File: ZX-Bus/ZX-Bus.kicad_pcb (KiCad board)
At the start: 2 copper layers, 177 x 146 mm, 56 parts, among them J1 DIP-40 Pins, J10 DIP14, J11 PBS-4, J12 PBS-5, J2 PLS-3, J3 PLS-6, J4 Power, J5 Main board power, J6 12V, J7 5V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

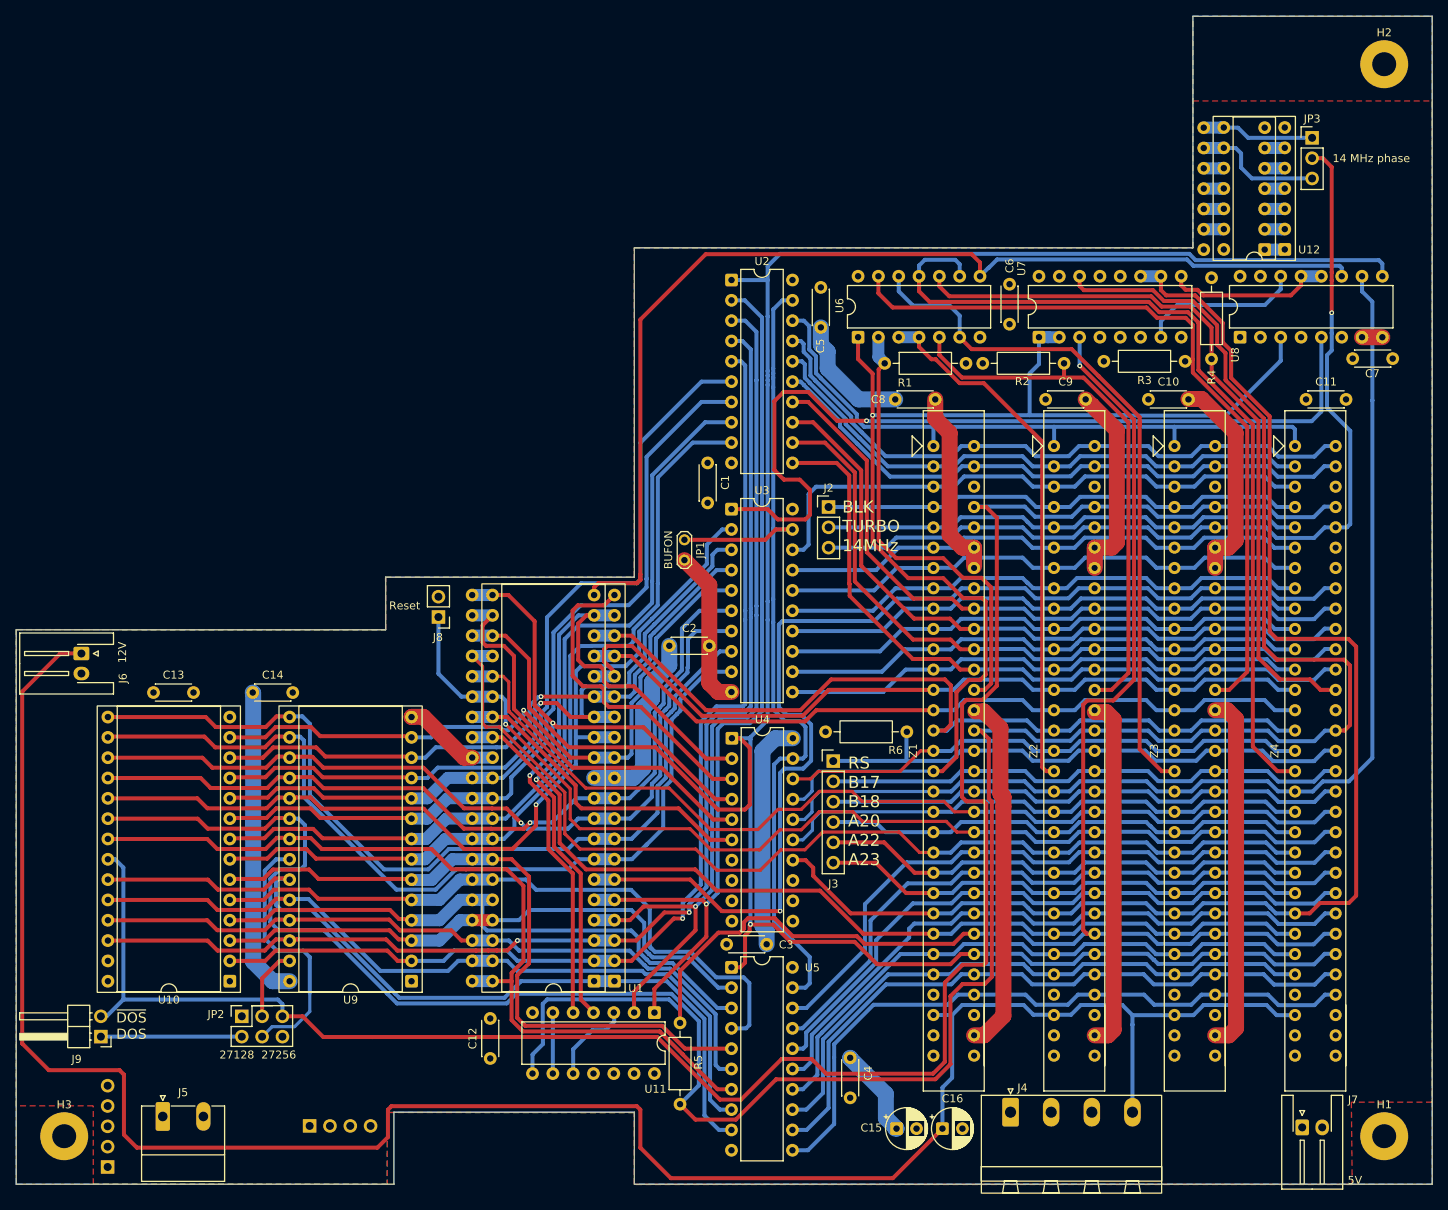
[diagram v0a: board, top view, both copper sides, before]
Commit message: ZX-Bus: Correct mounting hole placement
Based on mockup testing and re-measurement
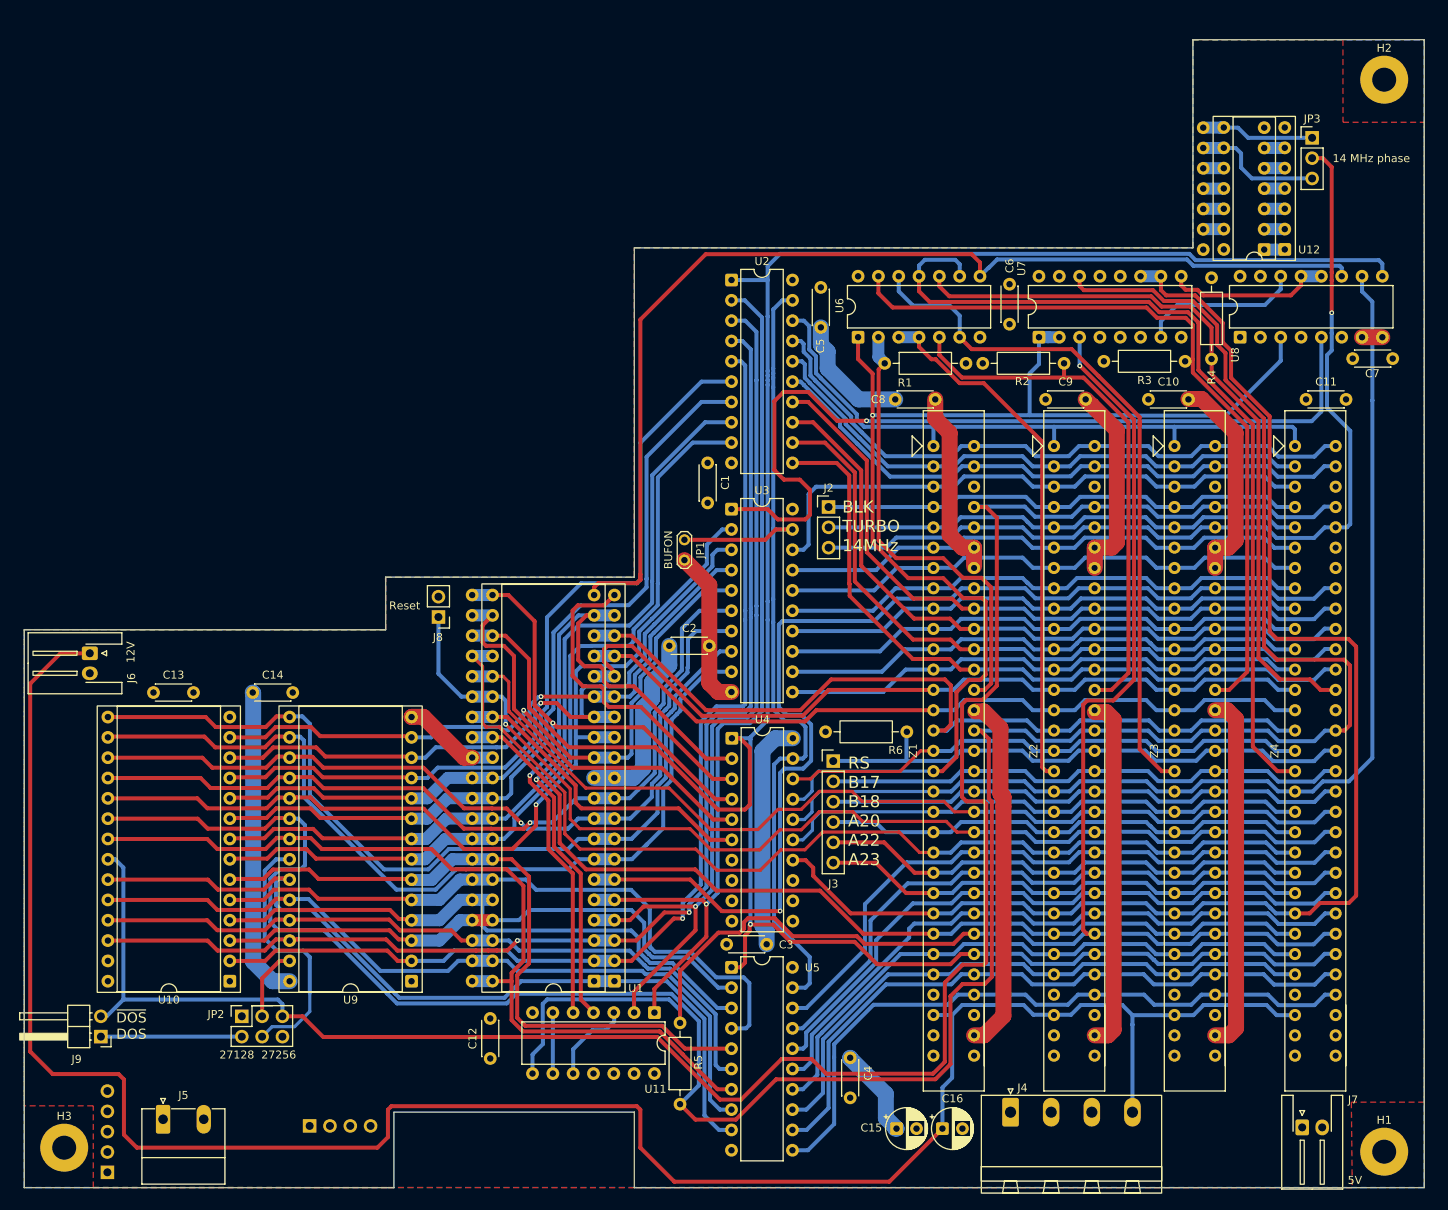
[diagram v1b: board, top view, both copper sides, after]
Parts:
- moved H1 1.94 mm to (186.8, 196.7)
- moved H2 1.94 mm to (186.8, 62.7)
- moved H3 1.44 mm to (21.8, 196.2)
- moved J6 1.05 mm to (25.0, 134.4)
- moved J12 0.67 mm to (27.2, 199.3)
- moved J5 0.35 mm to (34.1, 192.7)
- moved J10 0.06 mm to (171.8, 84.0)
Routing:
- net +12V: track 266.5 -> 265.7 mm
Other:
- board size 177 x 146 mm -> 175 x 143.5 mm

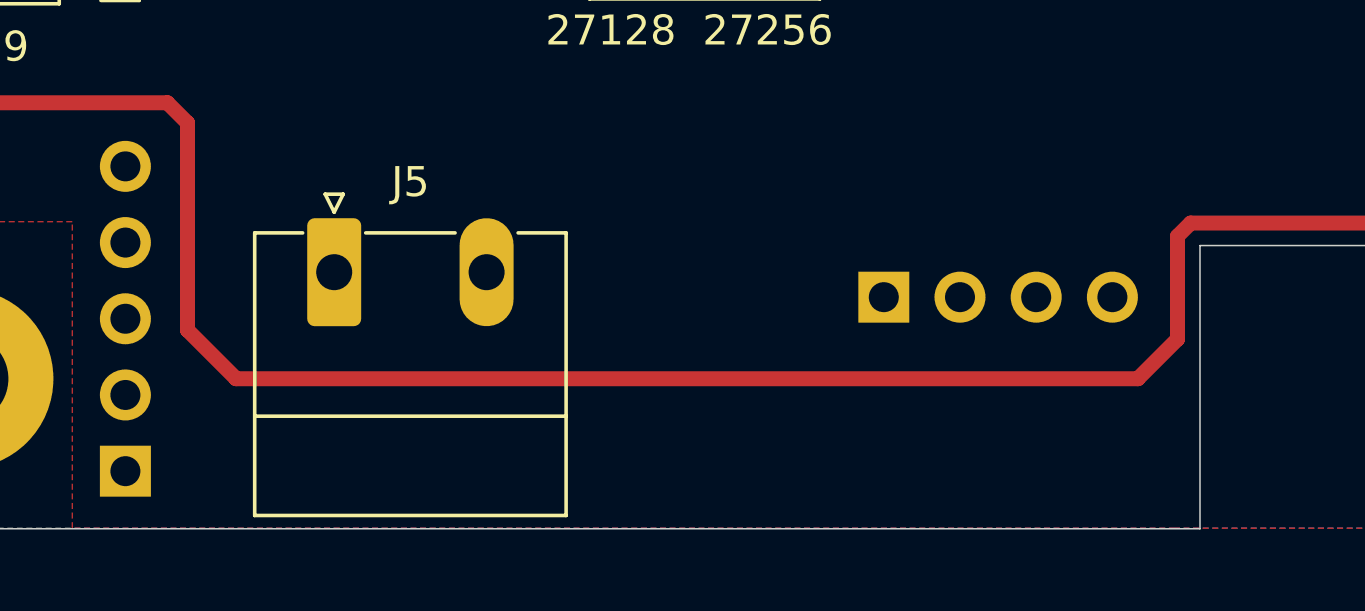
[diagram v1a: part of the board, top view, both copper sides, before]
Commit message: ZX-Bus: Adjust +5V connector position
Move by 0.5mm for easier soldering
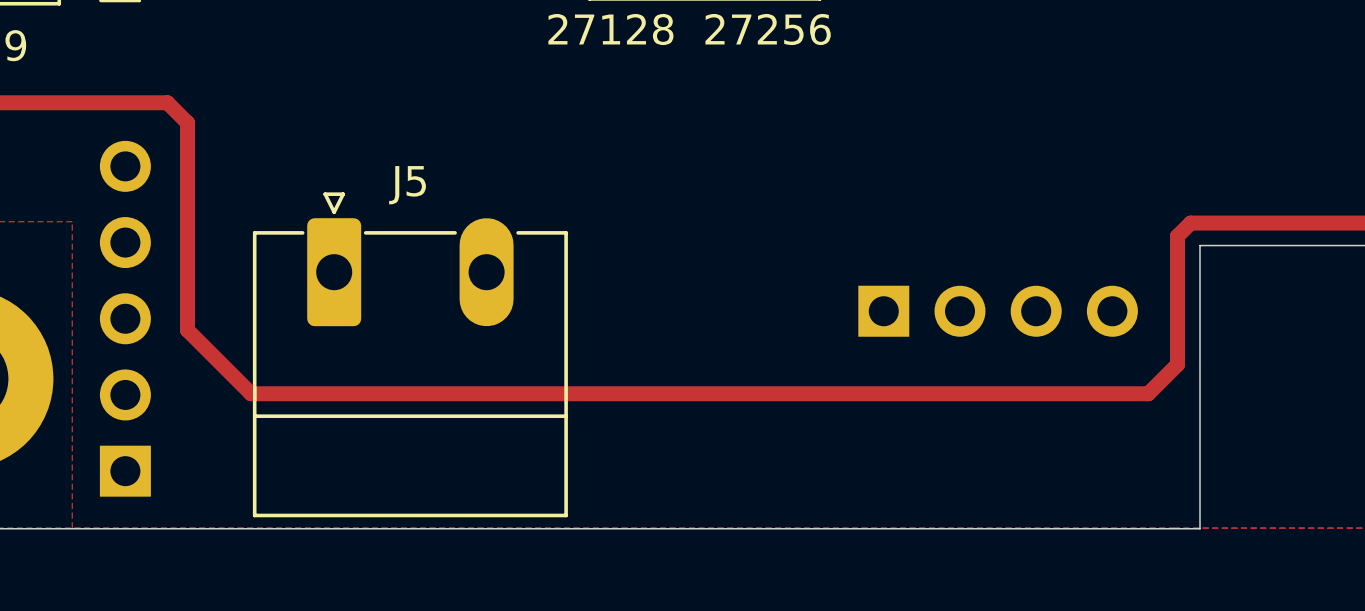
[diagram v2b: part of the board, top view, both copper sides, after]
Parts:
- moved J11 0.47 mm to (52.5, 194.0)
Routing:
- net +12V: track 265.7 -> 266.6 mm
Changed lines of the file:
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@@
 	(footprint "Connector_PinSocket_2.54mm:PinSocket_1x04_P2.54mm_Vertical"
 		(layer "B.Cu")
-		(at 52.4516 193.51675 -90)
+		(at 52.4516 193.98675 -90)
 		(descr "Through hole straight socket strip, 1x04, 2.54mm pitch, single row (from Kicad 4.0.7), script generated")
 		(tags "Through hole socket strip THT 1x04 2.54mm single row")
@@
 		(layer "Dwgs.User")
 		(pts
-			(xy 72.7716 175.41675) (xy 60.0716 193.51675)
+			(xy 72.7716 175.41675) (xy 60.0716 193.98675)
 		)
 		(height 33)
@@
 	)
 	(segment
-		(start 93.7908 191.48609)
-		(end 93.35146 191.04675)
+		(start 93.35146 191.04675)
+		(end 62.68094 191.04675)
 		(width 0.5)
 		(layer "F.Cu")
@@
 	)
 	(segment
-		(start 20.3368 187.03675)
-		(end 17.5216 184.22155)
+		(start 124.9164 200.48675)
+		(end 98.0368 200.48675)
 		(width 0.5)
 		(layer "F.Cu")
@@
 	)
 	(segment
-		(start 93.35146 191.04675)
-		(end 62.68094 191.04675)
+		(start 62.68094 191.04675)
+		(end 62.2416 191.48609)
 		(width 0.5)
 		(layer "F.Cu")
@@
 	)
 	(segment
-		(start 28.5716 187.03675)
-		(end 20.3368 187.03675)
+		(start 20.3368 187.03675)
+		(end 17.5216 184.22155)
 		(width 0.5)
 		(layer "F.Cu")
@@
 	)
 	(segment
-		(start 17.5216 184.22155)
-		(end 17.5216 138.23155)
+		(start 21.3016 134.45155)
+		(end 23.9064 134.45155)
 		(width 0.5)
 		(layer "F.Cu")
@@
 	)
 	(segment
-		(start 21.3016 134.45155)
-		(end 23.9064 134.45155)
+		(start 31.3616 196.73675)
+		(end 29.2416 194.61675)
 		(width 0.5)
 		(layer "F.Cu")
@@
 	)
 	(segment
-		(start 60.92235 196.236)
-		(end 30.86085 196.236)
+		(start 62.2416 195.76675)
+		(end 61.2716 196.73675)
 		(width 0.5)
 		(layer "F.Cu")
@@
 	)
 	(segment
-		(start 124.9164 200.48675)
-		(end 98.0368 200.48675)
+		(start 28.5716 187.03675)
+		(end 20.3368 187.03675)
 		(width 0.5)
 		(layer "F.Cu")
@@
 	)
 	(segment
-		(start 62.2416 194.91675)
-		(end 60.92235 196.236)
+		(start 98.0368 200.48675)
+		(end 93.7908 196.24075)
 		(width 0.5)
 		(layer "F.Cu")
@@
 	)
 	(segment
-		(start 98.0368 200.48675)
-		(end 93.7908 196.24075)
+		(start 131.5516 193.85155)
+		(end 124.9164 200.48675)
 		(width 0.5)
 		(layer "F.Cu")
@@
 	)
 	(segment
-		(start 30.86085 196.236)
-		(end 29.2416 194.61675)
+		(start 62.2416 191.48609)
+		(end 62.2416 195.76675)
 		(width 0.5)
 		(layer "F.Cu")
@@
 	)
 	(segment
-		(start 17.5216 138.23155)
-		(end 21.3016 134.45155)
+		(start 61.2716 196.73675)
+		(end 31.3616 196.73675)
 		(width 0.5)
 		(layer "F.Cu")
@@
 	)
 	(segment
-		(start 62.68094 191.04675)
-		(end 62.2416 191.48609)
+		(start 93.7908 191.48609)
+		(end 93.35146 191.04675)
 		(width 0.5)
 		(layer "F.Cu")
@@
 	)
 	(segment
-		(start 29.2416 194.61675)
-		(end 29.2416 187.70675)
+		(start 17.5216 184.22155)
+		(end 17.5216 138.23155)
 		(width 0.5)
 		(layer "F.Cu")
@@
 	)
 	(segment
-		(start 131.5516 193.85155)
-		(end 124.9164 200.48675)
+		(start 29.2416 194.61675)
+		(end 29.2416 187.70675)
 		(width 0.5)
 		(layer "F.Cu")
@@
 	)
 	(segment
-		(start 62.2416 191.48609)
-		(end 62.2416 194.91675)
+		(start 17.5216 138.23155)
+		(end 21.3016 134.45155)
 		(width 0.5)
 		(layer "F.Cu")
